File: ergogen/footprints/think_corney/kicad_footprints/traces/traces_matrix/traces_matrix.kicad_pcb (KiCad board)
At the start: 2 copper layers, 130.3 x 86.5 mm, 114 parts

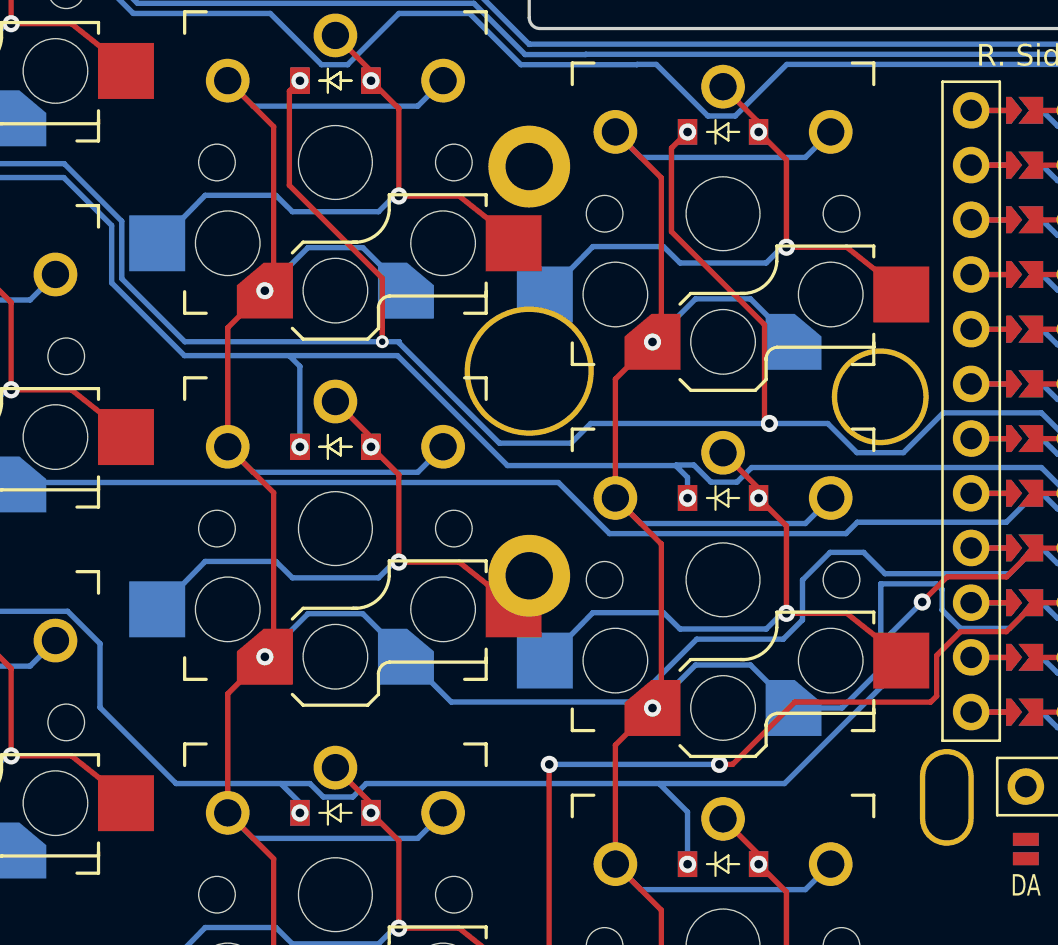
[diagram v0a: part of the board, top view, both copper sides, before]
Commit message: Traces: Fixed matrix traces for TP key changes
Added pcb
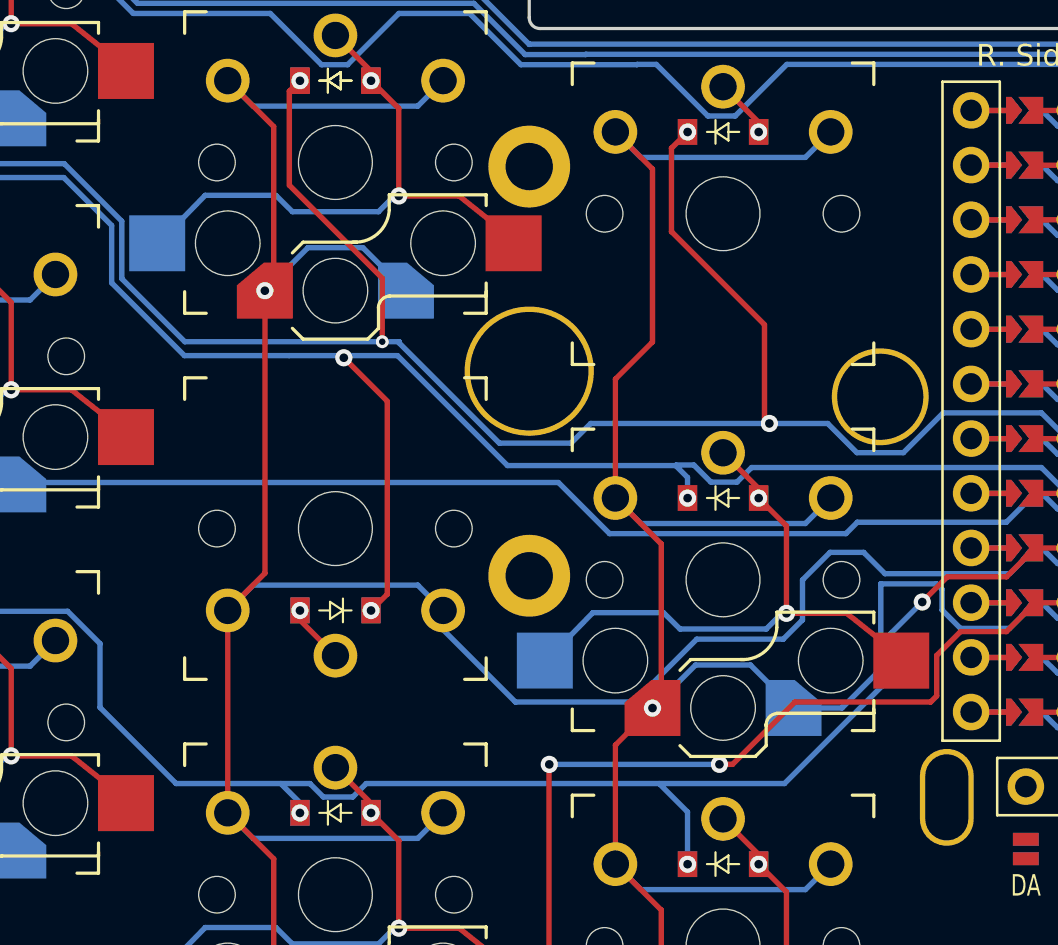
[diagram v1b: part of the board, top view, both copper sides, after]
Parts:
- removed D14, D22: , ComboDiode
- removed S10: , PG1350
- added D19: , ComboDiode, F.Cu at (-18.0, 18.4)
- added S19: , PG1350, F.Cu at (-18.0, 14.6)
- moved S20 23.2 mm to (0.00, 0.00), turned to 0 degrees
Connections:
- S20 pad 1: C4 -> C5
- S20 pad 2: index_home -> inner_top
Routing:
- net index_home: track 24.7 -> 2.78 mm, vias 2 -> 1
- net inner_top: track 24.7 -> 2.78 mm, vias 2 -> 1
- net C4: track 198.6 -> 188.4 mm, vias 4 -> 3
- net C5: track 182.8 -> 174.2 mm, vias 4 -> 3
- net R2: track 173.4 -> 181.8 mm, vias 6 -> 7

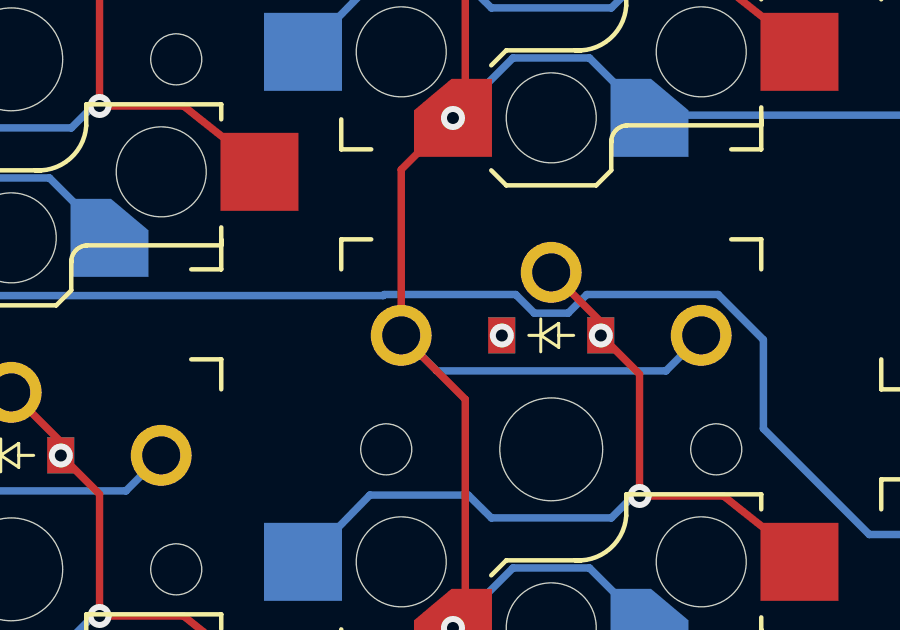
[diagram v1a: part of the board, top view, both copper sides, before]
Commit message: Traces: Added remaining missing traces
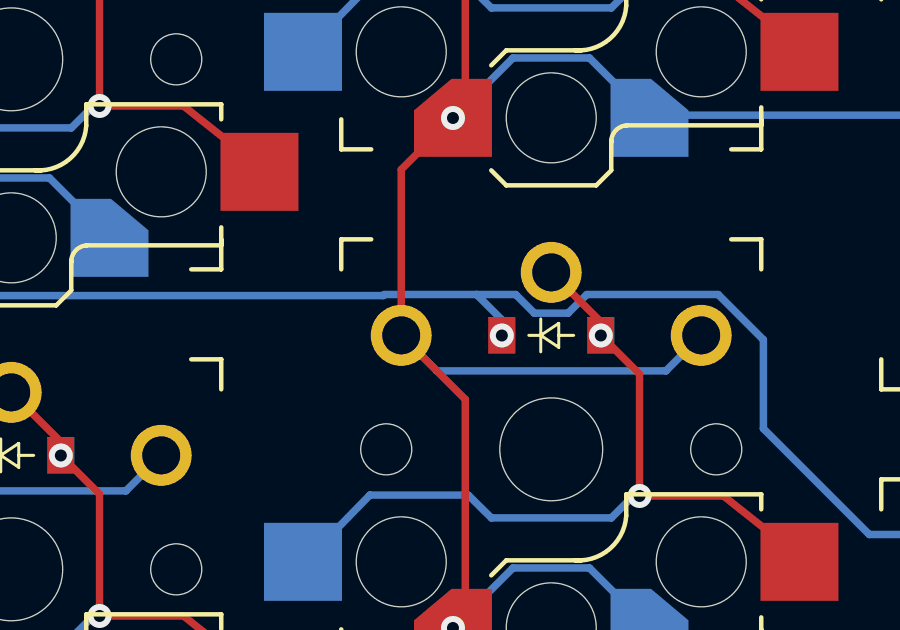
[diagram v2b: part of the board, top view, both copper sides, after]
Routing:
- net R3: track 169.9 -> 171.6 mm
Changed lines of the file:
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@@
   (segment (start -72.820864 40.163428) (end -73.101689 36.147445) (width 0.25) (layer "B.Cu") (net 19))
   (segment (start -64.933597 28.922268) (end -60.766736 24.755409) (width 0.25) (layer "B.Cu") (net 19))
-  (segment (start -41.563748 18.458991) (end -37.185748 18.458991) (width 0.25) (layer "B.Cu") (net 19))
   (segment (start -60.766737 22.41957) (end -60.766737 21.6234) (width 0.25) (layer "B.Cu") (net 19))
   (segment (start -76.530615 35.487222) (end -74.059932 35.314459) (width 0.25) (layer "B.Cu") (net 19))
+  (segment (start -37.645957 19.824695) (end -37.645957 19.303034) (width 0.25) (layer "B.Cu") (net 19))
   (segment (start -79.383263 44.169561) (end -78.728026 43.415797) (width 0.25) (layer "B.Cu") (net 19))
   (segment (start -90.94267 39.050088) (end -88.967507 36.777923) (width 0.25) (layer "B.Cu") (net 19))
@@
   (segment (start 7.794007 19.486205) (end 9.250644 18.029569) (width 0.25) (layer "B.Cu") (net 19))
   (segment (start -19.185748 26.458993) (end -18.563748 27.080994) (width 0.25) (layer "B.Cu") (net 19))
+  (segment (start -37.645957 19.303034) (end -38.49 18.458991) (width 0.25) (layer "B.Cu") (net 19))
   (segment locked (start 22.754037 14.794693) (end 22.054038 14.794696) (width 0.25) (layer "B.Cu") (net 19))
   (segment (start -64.740071 31.689813) (end -64.933597 28.922268) (width 0.25) (layer "B.Cu") (net 19))
@@
   (segment (start -20.539356 26.458993) (end -19.185748 26.458993) (width 0.25) (layer "B.Cu") (net 19))
   (segment locked (start 23.914038 15.52469) (end 23.474043 15.524695) (width 0.25) (layer "B.Cu") (net 19))
+  (segment (start -41.563748 18.458991) (end -38.49 18.458991) (width 0.25) (layer "B.Cu") (net 19))
   (segment (start -60.727312 22.458994) (end -60.766737 22.41957) (width 0.25) (layer "B.Cu") (net 19))
   (segment (start -55.650004 23.820003) (end -57.011012 22.458996) (width 0.25) (layer "B.Cu") (net 19))
+  (segment (start -38.49 18.458991) (end -37.185748 18.458991) (width 0.25) (layer "B.Cu") (net 19))
   (segment (start -28.928331 19.966919) (end -28.928331 22.930594) (width 0.25) (layer "B.Cu") (net 19))
   (segment (start 3.336074 22.675001) (end 9.639999 22.675001) (width 0.25) (layer "F.Cu") (net 20))
